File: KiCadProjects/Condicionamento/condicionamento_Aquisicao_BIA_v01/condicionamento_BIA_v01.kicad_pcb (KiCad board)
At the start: 2 copper layers, 90 x 100 mm, 27 parts, among them J1 Vref, J2 tensoes, J3 sinais analogicos, J4 comunicacao / sinais digitais, J5 sinais_condicionados, J6 Vmaster, J7 Eletrodos, U1 AD828AN, U2 BluePill_STM32F103C, U3 BluePill_STM32F103C_master

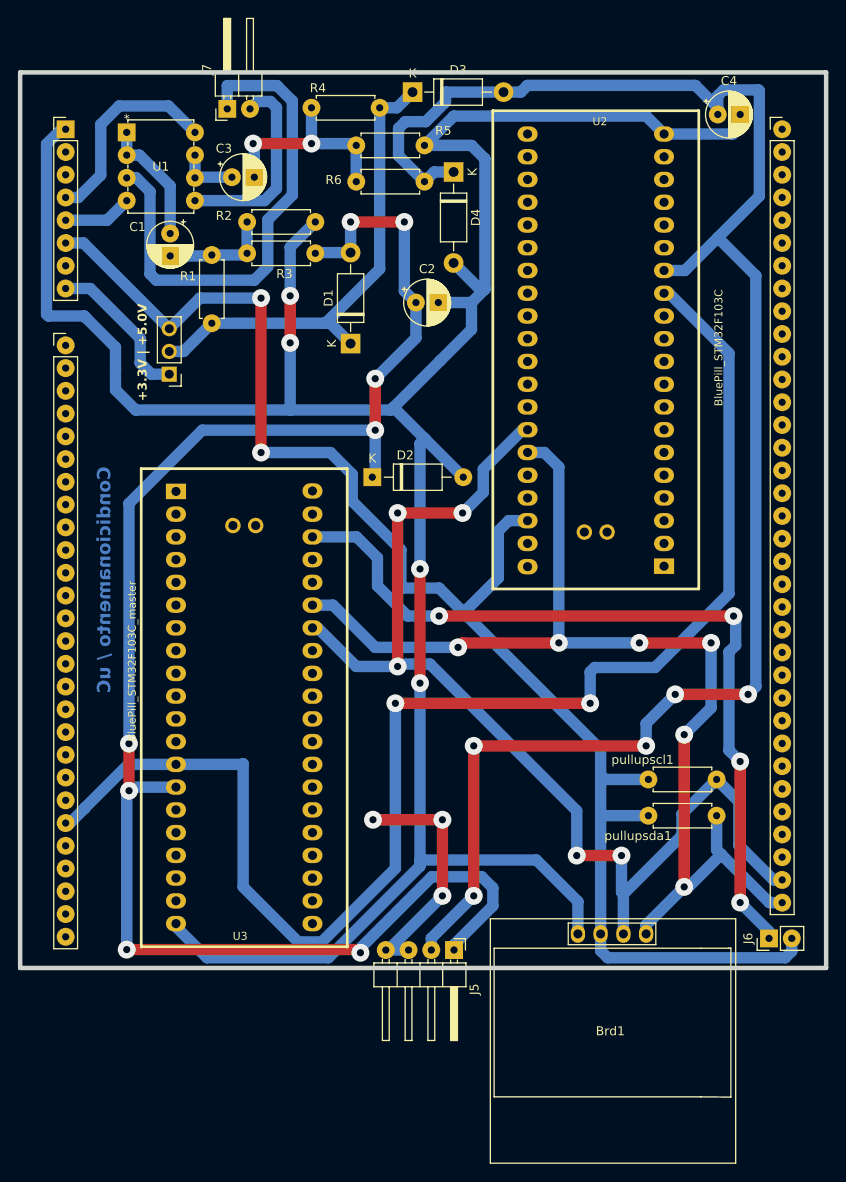
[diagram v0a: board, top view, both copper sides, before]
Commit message: correção polaridade capacitor condicionamento
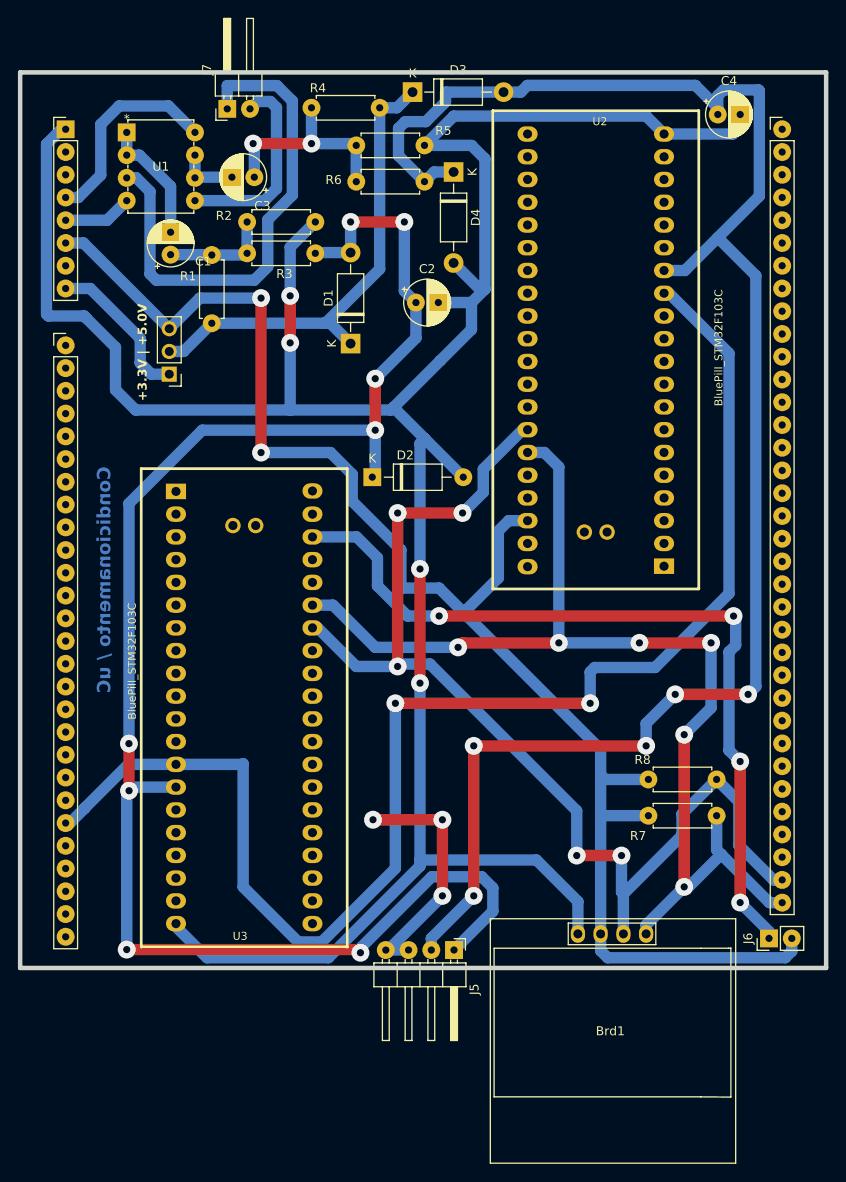
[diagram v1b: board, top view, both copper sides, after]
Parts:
- Brd1: value OLED -> SSD1306
- J6: value Vmaster -> alimetacao_Master
- U3: value BluePill_STM32F103C_master -> BluePill_STM32F103C
- moved C3 2.50 mm to (114.7, 60.2), turned to 180 degrees
- moved C1 2.36 mm to (105.3, 68.8), turned to 90 degrees
- renumbered pullupsda1 to R7, pullupscl1 to R8
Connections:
- C1 pad 1: nó1 -> nó2
- C1 pad 2: nó2 -> nó1
- C3 pad 1: nó3 -> nó4
- C3 pad 2: nó4 -> nó3
